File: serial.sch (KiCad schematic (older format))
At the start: 7 parts, among them J18 Conn_02x05_RS232, U8 MAX232

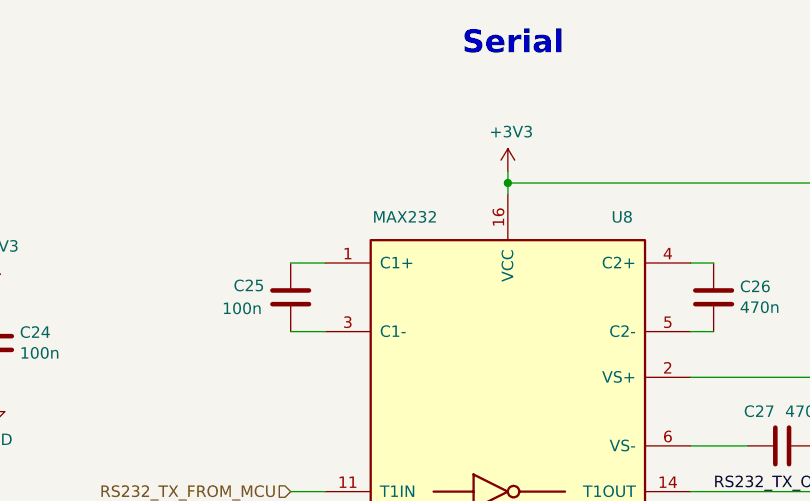
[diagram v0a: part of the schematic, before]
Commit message: Adding MPNs.
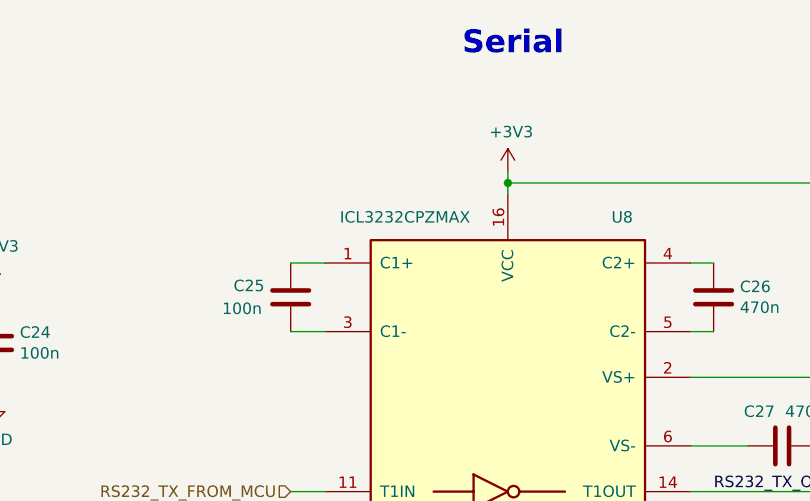
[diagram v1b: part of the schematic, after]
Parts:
- J18: Manufacturer (none) -> Harwin; PartNo (none) -> M20-9760546
- U8: value MAX232 -> ICL3232CPZMAX; Manufacturer (none) -> Renesas; PartNo (none) -> ICL3232CPZ
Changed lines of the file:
@@
 P 5600 3650
 F 0 "U8" H 6100 4750 50  0000 C CNN
-F 1 "MAX232" H 5150 4750 50  0000 C CNN
+F 1 "ICL3232CPZMAX" H 5150 4750 50  0000 C CNN
 F 2 "Package_DIP:DIP-16_W7.62mm" H 5650 2600 50  0001 L CNN
-F 3 "http://www.ti.com/lit/ds/symlink/max232.pdf" H 5600 3750 50  0001 C CNN
+F 3 "https://www.renesas.com/en-us/www/doc/datasheet/hin232-36-37-38-39-40-41.pdf" H 5600 3750 50  0001 C CNN
+F 4 "Renesas" H 5600 3650 50  0001 C CNN "Manufacturer"
+F 5 "ICL3232CPZ" H 5600 3650 50  0001 C CNN "PartNo"
 	1    5600 3650
 	1    0    0    -1
@@
 F 2 "Connector_PinHeader_2.54mm:PinHeader_2x05_P2.54mm_Vertical" H 8100 4050 50  0001 C CNN
 F 3 "~" H 8100 4050 50  0001 C CNN
+F 4 "Harwin" H 8100 4050 50  0001 C CNN "Manufacturer"
+F 5 "M20-9760546" H 8100 4050 50  0001 C CNN "PartNo"
 	1    8100 4050
 	1    0    0    1

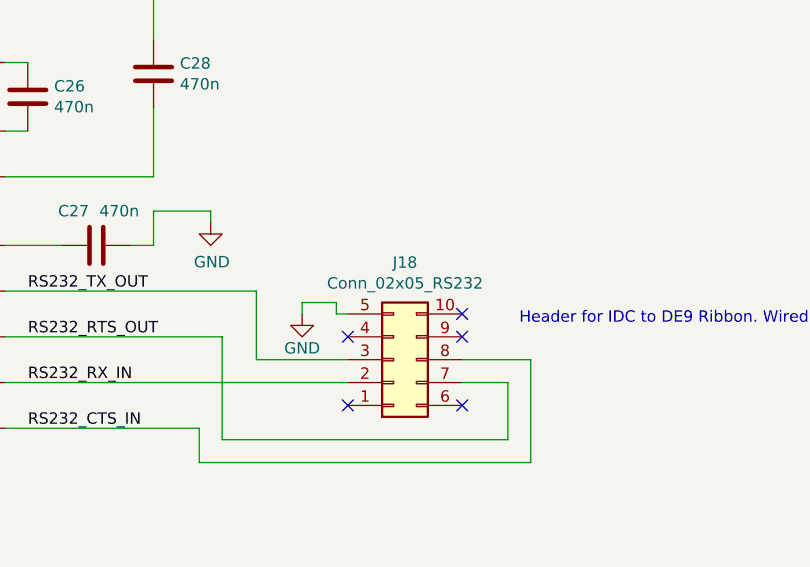
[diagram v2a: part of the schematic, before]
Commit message: Updated BOM.
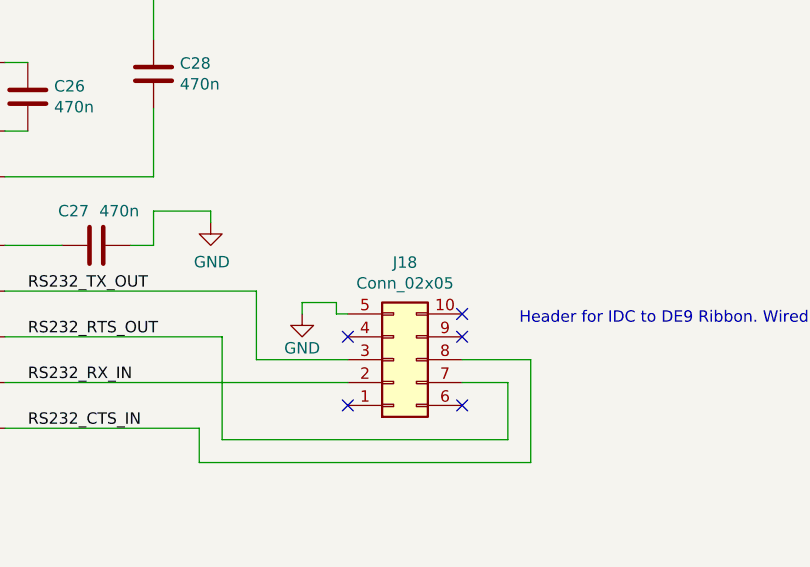
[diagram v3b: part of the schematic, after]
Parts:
- C24, C25: Manufacturer (none) -> Vishay; PartNo (none) -> K104K15X7RF5TL2
- C26, C27, C28: Manufacturer (none) -> Vishay; PartNo (none) -> K474Z20Y5VE5TL2
- J18: value Conn_02x05_RS232 -> Conn_02x05
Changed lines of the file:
@@
 F 2 "Capacitor_THT:C_Disc_D3.0mm_W2.0mm_P2.50mm" H 6538 2750 50  0001 C CNN
 F 3 "~" H 6500 2900 50  0001 C CNN
+F 4 "Vishay" H 0   0   50  0001 C CNN "Manufacturer"
+F 5 "K474Z20Y5VE5TL2" H 0   0   50  0001 C CNN "PartNo"
 	1    6500 2900
 	1    0    0    -1
@@
 F 2 "Capacitor_THT:C_Disc_D3.0mm_W2.0mm_P2.50mm" H 6838 3400 50  0001 C CNN
 F 3 "~" H 6800 3550 50  0001 C CNN
+F 4 "Vishay" H 0   0   50  0001 C CNN "Manufacturer"
+F 5 "K474Z20Y5VE5TL2" H 0   0   50  0001 C CNN "PartNo"
 	1    6800 3550
 	0    1    1    0
@@
 F 2 "Capacitor_THT:C_Disc_D3.0mm_W2.0mm_P2.50mm" H 4688 2750 50  0001 C CNN
 F 3 "~" H 4650 2900 50  0001 C CNN
+F 4 "Vishay" H 0   0   50  0001 C CNN "Manufacturer"
+F 5 "K104K15X7RF5TL2" H 0   0   50  0001 C CNN "PartNo"
 	1    4650 2900
 	-1   0    0    1
@@
 F 2 "Capacitor_THT:C_Disc_D3.0mm_W2.0mm_P2.50mm" H 3388 2950 50  0001 C CNN
 F 3 "~" H 3350 3100 50  0001 C CNN
+F 4 "Vishay" H 0   0   50  0001 C CNN "Manufacturer"
+F 5 "K104K15X7RF5TL2" H 0   0   50  0001 C CNN "PartNo"
 	1    3350 3100
 	-1   0    0    1
@@
 F 2 "Capacitor_THT:C_Disc_D3.0mm_W2.0mm_P2.50mm" H 7088 2650 50  0001 C CNN
 F 3 "~" H 7050 2800 50  0001 C CNN
+F 4 "Vishay" H 0   0   50  0001 C CNN "Manufacturer"
+F 5 "K474Z20Y5VE5TL2" H 0   0   50  0001 C CNN "PartNo"
 	1    7050 2800
 	1    0    0    -1
@@
 P 8100 4050
 F 0 "J18" H 8150 3625 50  0000 C CNN
-F 1 "Conn_02x05_RS232" H 8150 3716 50  0000 C CNN
+F 1 "Conn_02x05" H 8150 3716 50  0000 C CNN
 F 2 "Connector_PinHeader_2.54mm:PinHeader_2x05_P2.54mm_Vertical" H 8100 4050 50  0001 C CNN
 F 3 "~" H 8100 4050 50  0001 C CNN

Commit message: Add some extra explanatory notes.
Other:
- note added: "This chip is a 3.3V capable version of the MAX232 RS-232 level shifter. The port is wired DTE (i.e. as if this was an IBM PC, rather than\nas a modem). We only have a five-wire RS-232 interface, missing the Ring Input, Data Set Ready, Data Terminal Ready and Carrier Detect\npins.\n\nIf you want a proper DE9 RS-232 port, you will need a 10-way IDC ribbon to DE9 male cable. These were commonly fitt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"
- note removed: "Serial"
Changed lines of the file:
@@
 EESchema Schematic File Version 4
-LIBS:neotron-32-cache
-EELAYER 26 0
+EELAYER 30 0
 EELAYER END
 $Descr A4 11693 8268
@@
 Wire Wire Line
 	3350 3250 3350 3350
-Text Notes 5400 1850 0    100  ~ 20
-Serial
 NoConn ~ 8400 3850
 NoConn ~ 7900 4250
@@
 Text Notes 8650 3900 0    50   ~ 0
 Header for IDC to DE9 Ribbon. Wired DTE.
+Text Notes 550  7700 0    50   Italic 0
+This chip is a 3.3V capable version of the MAX232 RS-232 level shifter. The port is wired DTE (i.e. as if this was an IBM PC, rather than\nas a modem). We only have a five-wire RS-232 interface, missing the Ring Input, Data Set Ready, Data Terminal Ready and Carrier Detect\npins.\n\nIf you want a proper DE9 RS-232 port, you will need a 10-way IDC ribbon to DE9 male cable. These were commonly fitted to PCs in the 1990s\nas the ISA I/O expansion cards and/or motherboards of the time often didn't have room for all of the ports on the backplate. We didn't\nfit a DE9 to this board due to similar space issues.
 $EndSCHEMATC

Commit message: Moved non-standard components into local libraries.
neotron-32.lib is the symbol library.
neotron-32.pretty is the footprint library.

Also swapped the DE9 and DB25 headers for IDC boxed versions. Involved
moving a resistor out of the way.

The Keystone 103 battery holder is a straight copy of the standard
footprint, but with the Courtyard removed to bypass the 'Courtyard is
not closed' DRC error.
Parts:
- J18: footprint Connector_PinHeader_2.54mm:PinHeader_2x05_P2.54mm_Vertical -> Connector_IDC:IDC-Header_2x05_P2.54mm_Vertical
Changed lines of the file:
@@
 F 0 "J18" H 8150 3625 50  0000 C CNN
 F 1 "Conn_02x05" H 8150 3716 50  0000 C CNN
-F 2 "Connector_PinHeader_2.54mm:PinHeader_2x05_P2.54mm_Vertical" H 8100 4050 50  0001 C CNN
+F 2 "Connector_IDC:IDC-Header_2x05_P2.54mm_Vertical" H 8100 4050 50  0001 C CNN
 F 3 "~" H 8100 4050 50  0001 C CNN
 F 4 "Harwin" H 8100 4050 50  0001 C CNN "Manufacturer"
